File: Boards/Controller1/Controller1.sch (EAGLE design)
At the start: 9 parts

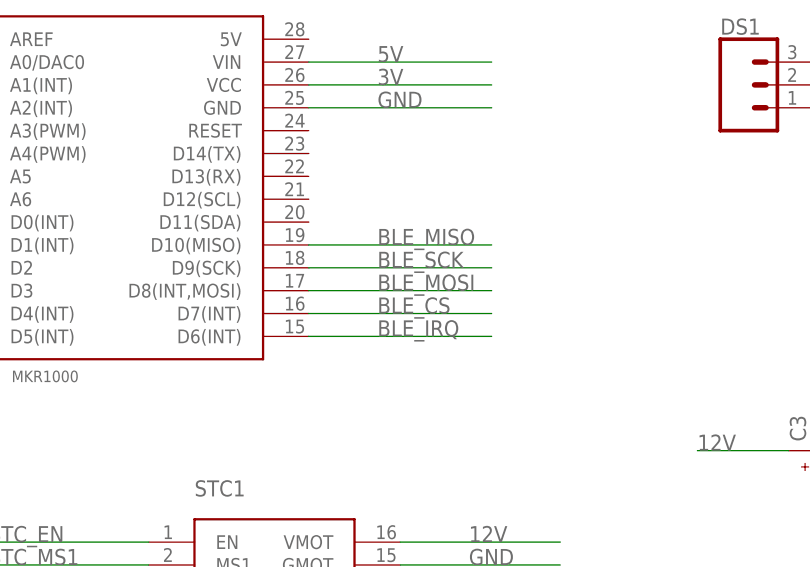
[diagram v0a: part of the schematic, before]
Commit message: removed obsolete signals
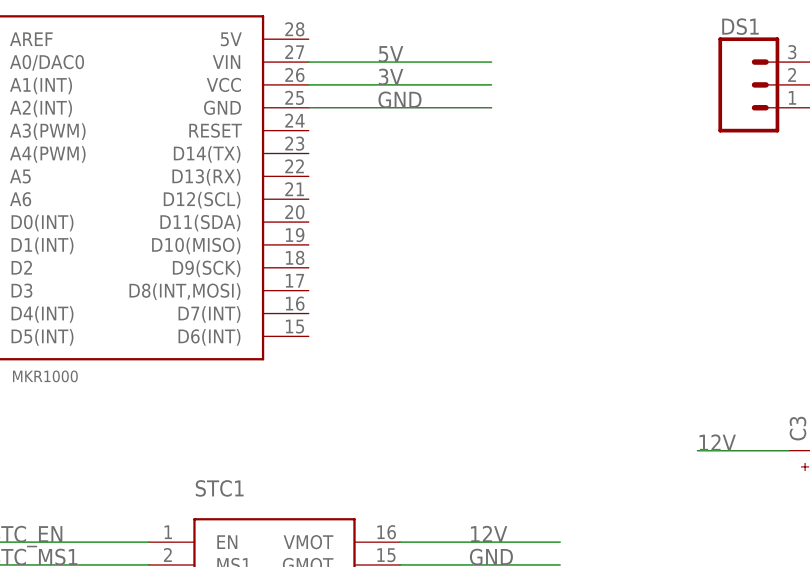
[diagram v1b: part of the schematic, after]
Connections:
- removed net BLE_CS: MCU1.D7(INT)
- removed net BLE_IRQ: MCU1.D6(INT)
- removed net BLE_MISO: MCU1.D10(MISO)
- removed net BLE_MOSI: MCU1.D8(INT,MOSI)
- removed net BLE_SCK: MCU1.D9(SCK)
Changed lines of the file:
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@@
 </busses>
 <nets>
-<net name="BLE_SCK" class="0">
-<segment>
-<pinref part="MCU1" gate="G$1" pin="D9(SCK)"/>
-<wire x1="50.8" y1="53.34" x2="71.12" y2="53.34" width="0.1524" layer="91"/>
-<label x="58.42" y="53.34" size="1.778" layer="95"/>
-</segment>
-</net>
-<net name="BLE_MISO" class="0">
-<segment>
-<pinref part="MCU1" gate="G$1" pin="D10(MISO)"/>
-<wire x1="50.8" y1="55.88" x2="71.12" y2="55.88" width="0.1524" layer="91"/>
-<label x="58.42" y="55.88" size="1.778" layer="95"/>
-</segment>
-</net>
-<net name="BLE_MOSI" class="0">
-<segment>
-<pinref part="MCU1" gate="G$1" pin="D8(INT,MOSI)"/>
-<wire x1="50.8" y1="50.8" x2="71.12" y2="50.8" width="0.1524" layer="91"/>
-<label x="58.42" y="50.8" size="1.778" layer="95"/>
-</segment>
-</net>
-<net name="BLE_CS" class="0">
-<segment>
-<pinref part="MCU1" gate="G$1" pin="D7(INT)"/>
-<wire x1="50.8" y1="48.26" x2="71.12" y2="48.26" width="0.1524" layer="91"/>
-<label x="58.42" y="48.26" size="1.778" layer="95"/>
-</segment>
-</net>
 <net name="GND" class="0">
 <segment>
@@
 </segment>
 </net>
-<net name="BLE_IRQ" class="0">
-<segment>
-<pinref part="MCU1" gate="G$1" pin="D6(INT)"/>
-<wire x1="50.8" y1="45.72" x2="71.12" y2="45.72" width="0.1524" layer="91"/>
-<label x="58.42" y="45.72" size="1.778" layer="95"/>
-</segment>
-</net>
